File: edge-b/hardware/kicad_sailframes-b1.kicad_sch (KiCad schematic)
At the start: 35 parts, among them J2 JST_PH_BAT, U2 TP4056, U3 MT3608

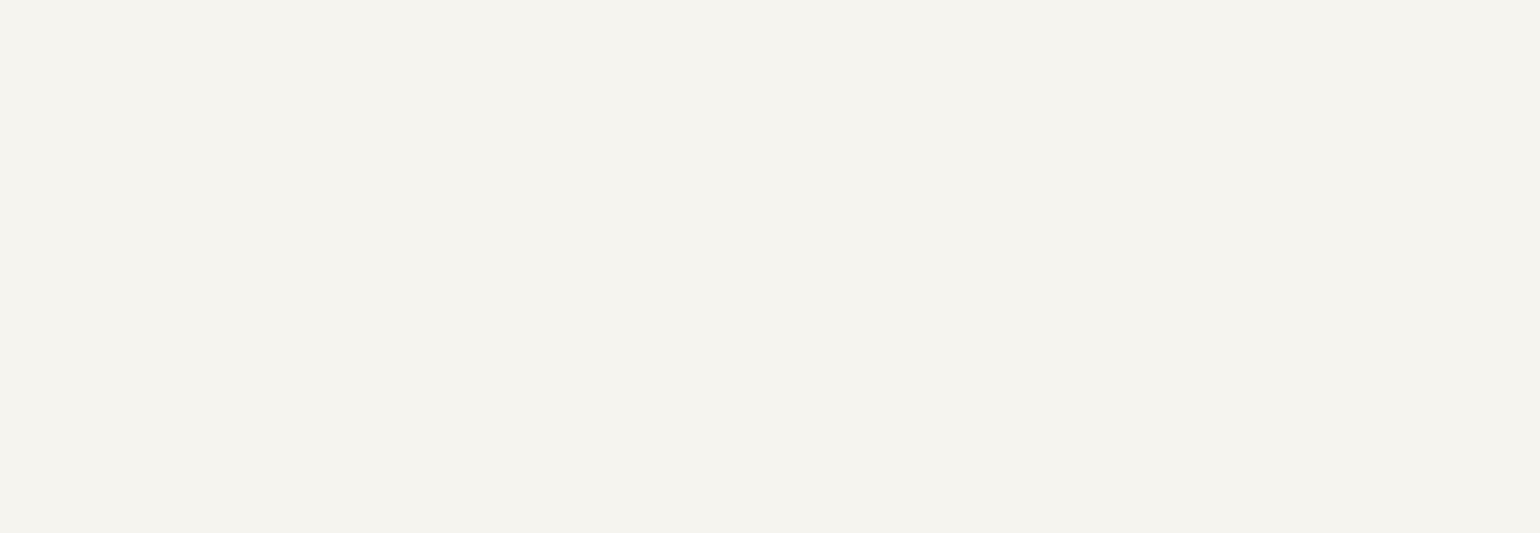
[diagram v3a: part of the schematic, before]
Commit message: B1 schematic Section 3: LC29HEAMD GNSS + bias-T + test pads
15 new components:
- U1 LC29HEAMD (24-pin LCC) — the dual-band L1/L5 GNSS module
- L2 33 nH bias-T inductor (L_BIAS, 0402) — spec checklist line 1261
  value (NOT 10 nH; X_L ≈ 326 Ω at L1, 244 Ω at L5)
- C10 10 nF (C_BYPASS, 0402) — RF bypass on VDD_RF side of L_BIAS
- C11 100 pF (C_BLOCK, 0402) — DC block between RF_IN and antenna feed
- C12/C13/C14 (10 uF + 100 nF + 10 nF) — VCC decoupling per spec
- D10 SS14 — V_BCKP backup Schottky from V3V3
- R16 10 k — RESET_N pull-up to V3V3
- J3 U.FL coaxial receptacle (Connector:Conn_Coaxial) — feed to antenna
- TP1/TP2/TP3/TP4 test pads (Connector:TestPoint) — TXD/RXD/RESET_N/GND
  exposed copper for firmware-update access via QGPSFlashTool

Bias-T topology verified:
- U1.9 (VDD_RF) - L2 - ANT_FEED - J3.1 (u.FL center)
- U1.11 (RF_IN) - C11 - ANT_FEED
- C10 from VDD_RF to GND (RF bypass)
- U1.23 (VCC) on V3V3 with C12/C13/C14 in parallel

12 LC29HEAMD pins marked no_connect:
- 1 WAKEUP, 2 FWD, 4 WHEELTICK (unused)
- 5/6/15/16/17 RESERVED (per datasheet)
- 7 VDD_EXT (1.8V external interface — not used)
- 14 ANT_ON (active antenna power gating — not used; YFGC007E3A is
  always on via the bias-T supply)
- 18 I2C_SDA, 19 I2C_SCL (1.8V level — not used)

Net cross-section additions:
- V3V3: 7 labels (was isolated PWR_FLAG only, now connected to U1.23,
  R16.1, D10.2 anode, C12/C13/C14 tops)
- GNSS_TXD: 2 labels (U1.20 + TP1) — second instance will be ESP32
  GPIO16 in Section 4
- GNSS_RXD: 2 (U1.21 + TP2)
- GNSS_RESET_N: 3 (U1.8 + R16.2 + TP3)
- GNSS_VDD_RF: 3 (U1.9 + L2.1 + C10.1)
- ANT_FEED: 3 (L2.2 + C11.1 + J3.1)
- GNSS_1PPS: 1 (U1.3 only — second instance will be ESP32 GPIO39 in
  Section 4; ERC isolated_pin_label warning expected until then)

Lib additions: Connector:Conn_Coaxial, Connector:TestPoint, and
B1_JLC:LC29HEAMD (was already in jlc_libs but not yet pulled into the
schematic's lib_symbols).

ERC after Section 3 (kicad-cli):
- pin_not_connected:    0
- u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
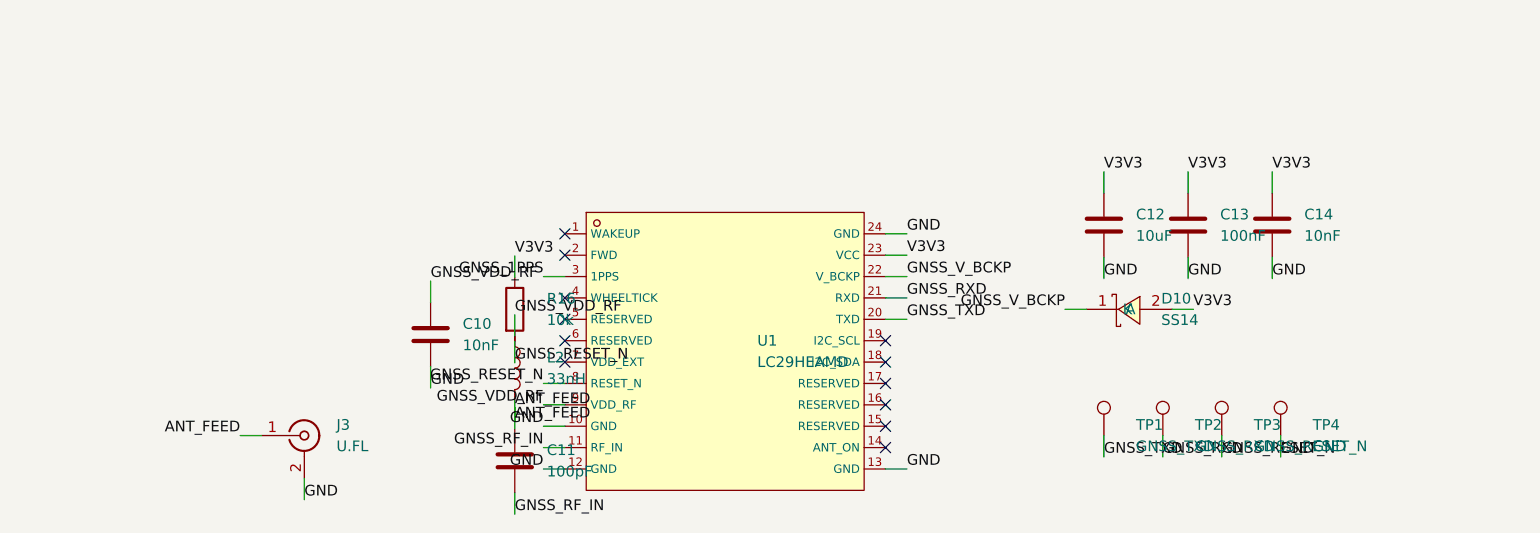
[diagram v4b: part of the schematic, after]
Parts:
- added C10: 10nF, Capacitor_SMD:C_0402_1005Metric, symbol Device:C
- added C11: 100pF, Capacitor_SMD:C_0402_1005Metric, symbol Device:C
- added C12: 10uF, Capacitor_SMD:C_0603_1608Metric, symbol Device:C
- added C13: 100nF, Capacitor_SMD:C_0603_1608Metric, symbol Device:C
- added C14: 10nF, Capacitor_SMD:C_0603_1608Metric, symbol Device:C
- added D10: SS14, Diode_SMD:D_SMA, symbol B1_SS14:SS14
- added J3: U.FL, Connector_Coaxial:U.FL_Hirose_U.FL-R-SMT-1_Vertical, symbol Connector:Conn_Coaxial
- added L2: 33nH, Inductor_SMD:L_0402_1005Metric, symbol Device:L
- added R16: 10k, Resistor_SMD:R_0603_1608Metric, symbol Device:R
- added TP1: GNSS_TXD, TestPoint:TestPoint_Pad_1.0x1.0mm, symbol Connector:TestPoint
- added TP2: GNSS_RXD, TestPoint:TestPoint_Pad_1.0x1.0mm, symbol Connector:TestPoint
- added TP3: GNSS_RESET_N, TestPoint:TestPoint_Pad_1.0x1.0mm, symbol Connector:TestPoint
- added TP4: GND, TestPoint:TestPoint_Pad_1.0x1.0mm, symbol Connector:TestPoint
- added U1: LC29HEAMD, Package_LCC:LCC-24_4x4mm_P0.5mm, symbol B1_JLC:LC29HEAMD
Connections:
- net GND: now also C10.2, C12.2, C13.2, C14.2, J3.2 (Ext), TP4.1, U1.10 (GND), U1.12 (GND), U1.13 (GND), U1.24 (GND)
- net V3V3: now also C12.1, C13.1, C14.1, D10.2 (A), R16.1, U1.23 (VCC)
- new net ANT_FEED: C11.1, J3.1 (In), L2.2
- new net GNSS_1PPS: U1.3 (1PPS)
- new net GNSS_RESET_N: R16.2, TP3.1, U1.8 (RESET_N)
- new net GNSS_RF_IN: C11.2, U1.11 (RF_IN)
- new net GNSS_RXD: TP2.1, U1.21 (RXD)
- new net GNSS_TXD: TP1.1, U1.20 (TXD)
- new net GNSS_VDD_RF: C10.1, L2.1, U1.9 (VDD_RF)
- new net GNSS_V_BCKP: D10.1 (K), U1.22 (V_BCKP)
- no-connect marks 2 -> 14
